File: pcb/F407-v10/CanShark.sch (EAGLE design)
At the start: 135 parts, among them IC1 STM32F407V, IC2 KSZ8051MLL, K2 JACK_POWER_2,1, U1 SN65HVD230DR, U2 SN65HVD230DR, U3 LM2594M-ADJ, U4 LM2594M-ADJ, U5 TSH24IDT, U6 MCP602-E/SN

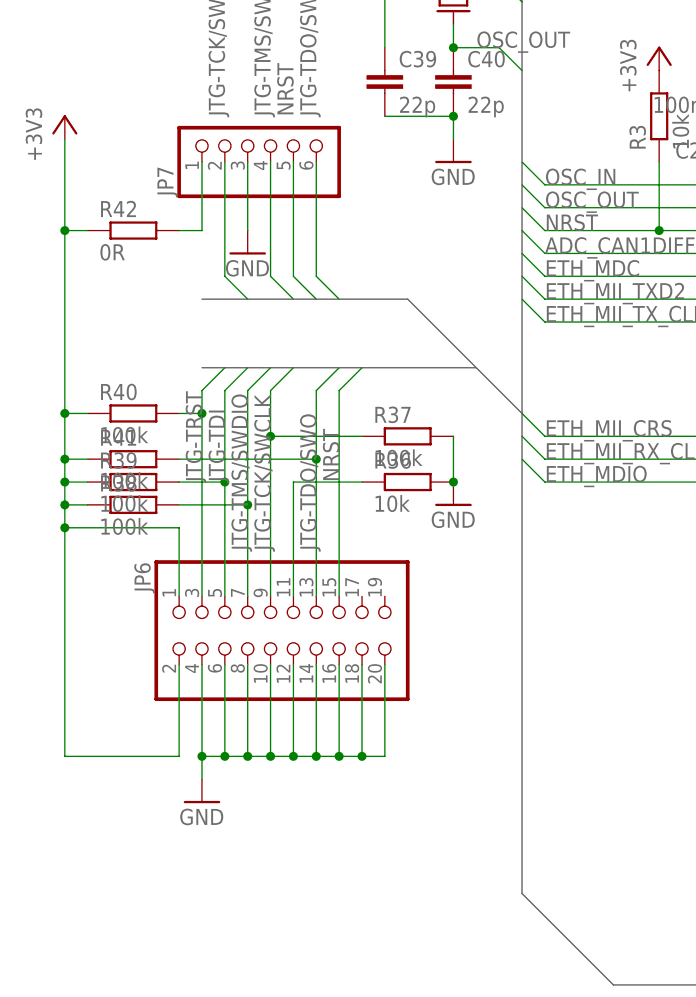
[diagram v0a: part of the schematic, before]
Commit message: remove JTAG connector,
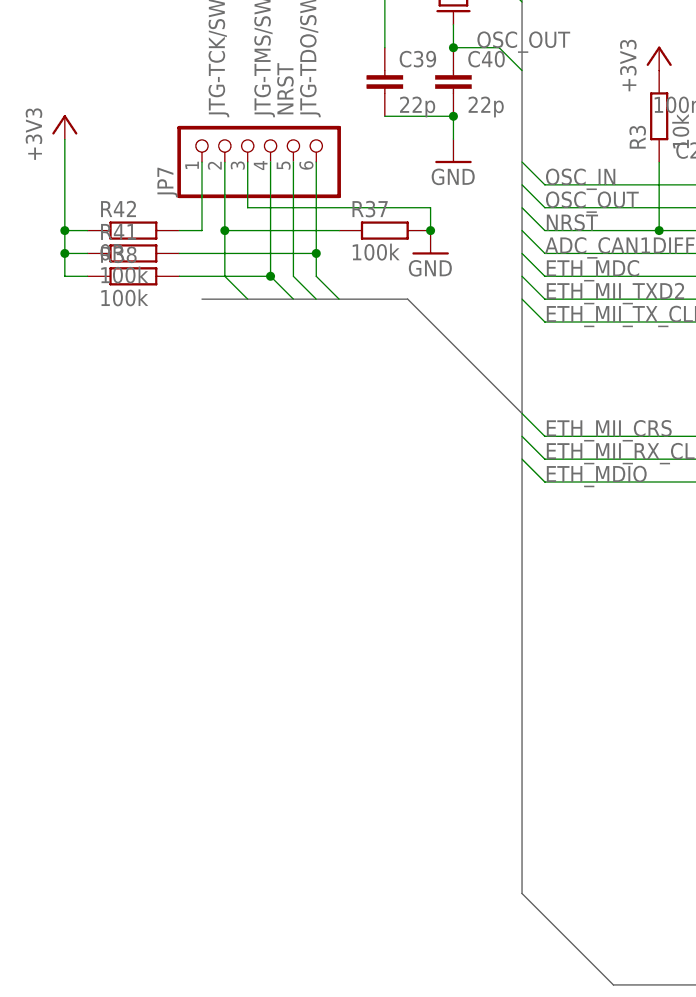
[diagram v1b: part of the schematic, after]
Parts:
- removed JP6: (no value), pinhead:PINHD-2X10
- removed R36: 10k, #Odpory:R-EU_R0603
- removed R39, R40: 100k, #Odpory:R-EU_R0603
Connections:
- removed net N$8: JP6.11, R36.1
- net +3V3: no longer JP6.1, JP6.2, R39.1, R40.1
- net GND: no longer JP6.10, JP6.12, JP6.14, JP6.16, JP6.18, JP6.20, JP6.4, JP6.6, JP6.8, R36.2
- net JTG-TCK/SWCLK: no longer JP6.9
- net JTG-TDI: no longer JP6.5, R39.2
- net JTG-TDO/SWO: no longer JP6.13
- net JTG-TMS/SWDIO: no longer JP6.7
- net JTG-TRST: no longer JP6.3, R40.2
- net NRST: no longer JP6.15
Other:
- moved on the sheet: R37, R38, R41
